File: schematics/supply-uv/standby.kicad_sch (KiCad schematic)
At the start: 108 parts, among them J5 CW2B-10A-T, K1 SRD-12VDC-SL-C, Q1 5N65F, Q2 IRLML5203, Q3 IRLML5203, Q4 IRLML5203, U10 TL331, U2 R7731, U3 EL817, U4 EL817, U5 L7805ABV, U6 L7805ABV, U7 TL431DBZ, U8 EL817, U9 TL432DBZ, Y1 B32022A3223M000

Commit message: Boards prepared to order
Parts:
- added TP3: Supply GND, Library:TestPoint_Plated_Hole_D1.0mm, symbol Connector:TestPoint
- TP10: renamed from TP8; footprint TestPoint:TestPoint_Pad_2.0x2.0mm -> TestPoint:TestPoint_Pad_1.0x1.0mm
- TP2: footprint TestPoint:TestPoint_Pad_2.0x2.0mm -> TestPoint:TestPoint_Pad_1.0x1.0mm
- TP5: renamed from TP4; footprint TestPoint:TestPoint_Pad_2.0x2.0mm -> TestPoint:TestPoint_Pad_1.0x1.0mm
- TP7: renamed from TP6; footprint TestPoint:TestPoint_Pad_2.0x2.0mm -> TestPoint:TestPoint_Pad_1.0x1.0mm
- renumbered C76 to C27, C27 to C28, C28 to C29, C29 to C30, R9 to R8, R8 to R9, TP9 to TP11, TP3 to TP4, TP5 to TP6, TP7 to TP8, TP35 to TP9
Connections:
- net HV_GND: now also TP3.1
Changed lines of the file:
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@@
 	(wire
 		(pts
+			(xy 87.63 236.22) (xy 111.76 236.22)
+		)
+		(stroke
+			(width 0)
+			(type default)
+		)
+	)
+	(wire
+		(pts
 			(xy 116.84 172.72) (xy 124.46 172.72)
 		)
@@
 	(wire
 		(pts
-			(xy 88.9 234.95) (xy 99.06 234.95)
+			(xy 88.9 224.79) (xy 99.06 224.79)
 		)
 		(stroke
@@
 		)
 	)
+	(hierarchical_label "HV_GND"
+		(shape input)
+		(at 87.63 236.22 180)
+		(fields_autoplaced yes)
+		(effects
+			(font
+				(size 1.27 1.27)
+			)
+			(justify right)
+		)
+	)
 	(hierarchical_label "VSYS1_VCC"
 		(shape input)
@@
 	(hierarchical_label "STB_VCC"
 		(shape input)
-		(at 88.9 234.95 180)
+		(at 88.9 224.79 180)
 		(fields_autoplaced yes)
 		(effects
@@
 		(dnp no)
 		(fields_autoplaced yes)
-		(property "Reference" "TP8"
+		(property "Reference" "TP10"
 			(at 163.83 34.7979 0)
 			(effects
@@
 			)
 		)
-		(property "Footprint" "TestPoint:TestPoint_Pad_2.0x2.0mm"
+		(property "Footprint" "TestPoint:TestPoint_Pad_1.0x1.0mm"
 			(at 166.37 39.37 0)
 			(effects
@@
 			(project ""
 				(path "/ef40850c-d0bf-4cba-961b-9aba418f8e73/14317b0a-1f8a-4d8b-b159-cbc20c410ffd"
-					(reference "TP8")
+					(reference "TP10")
 					(unit 1)
 				)
@@
 	(symbol
 		(lib_id "power:PWR_FLAG")
-		(at 99.06 234.95 0)
+		(at 99.06 224.79 0)
 		(unit 1)
 		(exclude_from_sim no)
@@
 		(fields_autoplaced yes)
 		(property "Reference" "#FLG03"
-			(at 99.06 233.045 0)
+			(at 99.06 222.885 0)
 			(effects
 				(font
@@
 		)
 		(property "Value" "PWR_FLAG"
-			(at 99.06 229.87 0)
+			(at 99.06 219.71 0)
 			(effects
 				(font
@@
 		)
 		(property "Footprint" ""
-			(at 99.06 234.95 0)
+			(at 99.06 224.79 0)
 			(effects
 				(font
@@
 		)
 		(property "Datasheet" "~"
-			(at 99.06 234.95 0)
+			(at 99.06 224.79 0)
 			(effects
 				(font
@@
 		)
 		(property "Description" "Special symbol for telling ERC where power comes from"
-			(at 99.06 234.95 0)
+			(at 99.06 224.79 0)
 			(effects
 				(font
@@
 		(dnp no)
 		(fields_autoplaced yes)
-		(property "Reference" "TP4"
+		(property "Reference" "TP5"
 			(at 114.3 245.6179 0)
 			(effects
@@
 			)
 		)
-		(property "Footprint" "TestPoint:TestPoint_Pad_2.0x2.0mm"
+		(property "Footprint" "TestPoint:TestPoint_Pad_1.0x1.0mm"
 			(at 116.84 250.19 0)
 			(effects
@@
 			(project "supply-uv"
 				(path "/ef40850c-d0bf-4cba-961b-9aba418f8e73/14317b0a-1f8a-4d8b-b159-cbc20c410ffd"
-					(reference "TP4")
+					(reference "TP5")
 					(unit 1)
 				)
@@
 		(on_board yes)
 		(dnp no)
-		(property "Reference" "R9"
+		(property "Reference" "R8"
 			(at 104.14 170.18 90)
 			(effects
@@
 			(project "supply-uv"
 				(path "/ef40850c-d0bf-4cba-961b-9aba418f8e73/14317b0a-1f8a-4d8b-b159-cbc20c410ffd"
-					(reference "R9")
+					(reference "R8")
 					(unit 1)
 				)
@@
 	)
 	(symbol
+		(lib_id "Connector:TestPoint")
+		(at 111.76 236.22 0)
+		(unit 1)
+		(exclude_from_sim no)
+		(in_bom yes)
+		(on_board yes)
+		(dnp no)
+		(fields_autoplaced yes)
+		(property "Reference" "TP3"
+			(at 114.3 231.6479 0)
+			(effects
+				(font
+					(size 1.27 1.27)
+				)
+				(justify left)
+			)
+		)
+		(property "Value" "Supply GND"
+			(at 114.3 234.1879 0)
+			(effects
+				(font
+					(size 1.27 1.27)
+				)
+				(justify left)
+			)
+		)
+		(property "Footprint" "Library:TestPoint_Plated_Hole_D1.0mm"
+			(at 116.84 236.22 0)
+			(effects
+				(font
+					(size 1.27 1.27)
+				)
+				(hide yes)
+			)
+		)
+		(property "Datasheet" "~"
+			(at 116.84 236.22 0)
+			(effects
+				(font
+					(size 1.27 1.27)
+				)
+				(hide yes)
+			)
+		)
+		(property "Description" "test point"
+			(at 111.76 236.22 0)
+			(effects
+				(font
+					(size 1.27 1.27)
+				)
+				(hide yes)
+			)
+		)
+		(pin "1"
+		)
+		(instances
+			(project "supply-uv"
+				(path "/ef40850c-d0bf-4cba-961b-9aba418f8e73/14317b0a-1f8a-4d8b-b159-cbc20c410ffd"
+					(reference "TP3")
+					(unit 1)
+				)
+			)
+		)
+	)
+	(symbol
 		(lib_id "Device:C_Polarized")
 		(at 370.84 135.89 0)
@@
 		(dnp no)
 		(fields_autoplaced yes)
-		(property "Reference" "C29"
+		(property "Reference" "C30"
 			(at 374.65 133.731 0)
 			(effects
@@
 			(project "supply-uv"
 				(path "/ef40850c-d0bf-4cba-961b-9aba418f8e73/14317b0a-1f8a-4d8b-b159-cbc20c410ffd"
-					(reference "C29")
+					(reference "C30")
 					(unit 1)
 				)
@@
 		(on_board yes)
 		(dnp no)
-		(property "Reference" "C27"
+		(property "Reference" "C28"
 			(at 340.36 148.59 0)
 			(effects
@@
 			(project "supply-uv"
 				(path "/ef40850c-d0bf-4cba-961b-9aba418f8e73/14317b0a-1f8a-4d8b-b159-cbc20c410ffd"
-					(reference "C27")
+					(reference "C28")
 					(unit 1)
 				)
@@
 		(dnp no)
 		(fields_autoplaced yes)
-		(property "Reference" "TP3"
+		(property "Reference" "TP4"
 			(at 114.3 239.2679 0)
 			(effects
@@
 			(project "supply-uv"
 				(path "/ef40850c-d0bf-4cba-961b-9aba418f8e73/14317b0a-1f8a-4d8b-b159-cbc20c410ffd"
-					(reference "TP3")
+					(reference "TP4")
 					(unit 1)
 				)
@@
 		(dnp no)
 		(fields_autoplaced yes)
-		(property "Reference" "TP9"
+		(property "Reference" "TP11"
 			(at 276.86 116.078 0)
 			(effects
@@
 			(project "supply-uv"
 				(path "/ef40850c-d0bf-4cba-961b-9aba418f8e73/14317b0a-1f8a-4d8b-b159-cbc20c410ffd"
-					(reference "TP9")
+					(reference "TP11")
 					(unit 1)
 				)
@@
 		(on_board yes)
 		(dnp no)
-		(property "Reference" "C76"
+		(property "Reference" "C27"
 			(at 281.178 369.57 0)
 			(effects
@@
 			(project "supply-uv"
 				(path "/ef40850c-d0bf-4cba-961b-9aba418f8e73/14317b0a-1f8a-4d8b-b159-cbc20c410ffd"
-					(reference "C76")
+					(reference "C27")
 					(unit 1)
 				)
@@
 		(dnp no)
 		(fields_autoplaced yes)
-		(property "Reference" "TP7"
+		(property "Reference" "TP8"
 			(at 114.3 268.4779 0)
 			(effects
@@
 			(project "supply-uv"
 				(path "/ef40850c-d0bf-4cba-961b-9aba418f8e73/14317b0a-1f8a-4d8b-b159-cbc20c410ffd"
-					(reference "TP7")
+					(reference "TP8")
 					(unit 1)
 				)
@@
 		(dnp no)
 		(fields_autoplaced yes)
-		(property "Reference" "TP5"
+		(property "Reference" "TP6"
 			(at 114.3 253.2379 0)
 			(effects
@@
 			(project "supply-uv"
 				(path "/ef40850c-d0bf-4cba-961b-9aba418f8e73/14317b0a-1f8a-4d8b-b159-cbc20c410ffd"
-					(reference "TP5")
+					(reference "TP6")
 					(unit 1)
 				)
@@
 		(on_board yes)
 		(dnp no)
-		(property "Reference" "TP35"
+		(property "Reference" "TP9"
 			(at 113.792 165.608 0)
 			(effects
@@
 			(project "supply-uv"
 				(path "/ef40850c-d0bf-4cba-961b-9aba418f8e73/14317b0a-1f8a-4d8b-b159-cbc20c410ffd"
-					(reference "TP35")
+					(reference "TP9")
 					(unit 1)
 				)
@@
 		(on_board yes)
 		(dnp no)
-		(property "Reference" "C28"
+		(property "Reference" "C29"
 			(at 345.44 238.125 0)
 			(effects
@@
 			(project "supply-uv"
 				(path "/ef40850c-d0bf-4cba-961b-9aba418f8e73/14317b0a-1f8a-4d8b-b159-cbc20c410ffd"
-					(reference "C28")
+					(reference "C29")
 					(unit 1)
 				)
@@
 		(dnp no)
 		(fields_autoplaced yes)
-		(property "Reference" "TP6"
+		(property "Reference" "TP7"
 			(at 114.3 260.8579 0)
 			(effects
@@
 			)
 		)
-		(property "Footprint" "TestPoint:TestPoint_Pad_2.0x2.0mm"
+		(property "Footprint" "TestPoint:TestPoint_Pad_1.0x1.0mm"
 			(at 116.84 265.43 0)
 			(effects
@@
 			(project "supply-uv"
 				(path "/ef40850c-d0bf-4cba-961b-9aba418f8e73/14317b0a-1f8a-4d8b-b159-cbc20c410ffd"
-					(reference "TP6")
+					(reference "TP7")
 					(unit 1)
 				)
@@
 		(on_board yes)
 		(dnp no)
-		(property "Reference" "R8"
+		(property "Reference" "R9"
 			(at 102.87 133.35 0)
 			(effects
@@
 			(project "supply-uv"
 				(path "/ef40850c-d0bf-4cba-961b-9aba418f8e73/14317b0a-1f8a-4d8b-b159-cbc20c410ffd"
-					(reference "R8")
+					(reference "R9")
 					(unit 1)
 				)
@@
 			)
 		)
-		(property "Footprint" "TestPoint:TestPoint_Pad_2.0x2.0mm"
+		(property "Footprint" "TestPoint:TestPoint_Pad_1.0x1.0mm"
 			(at 96.52 143.51 0)
 			(effects

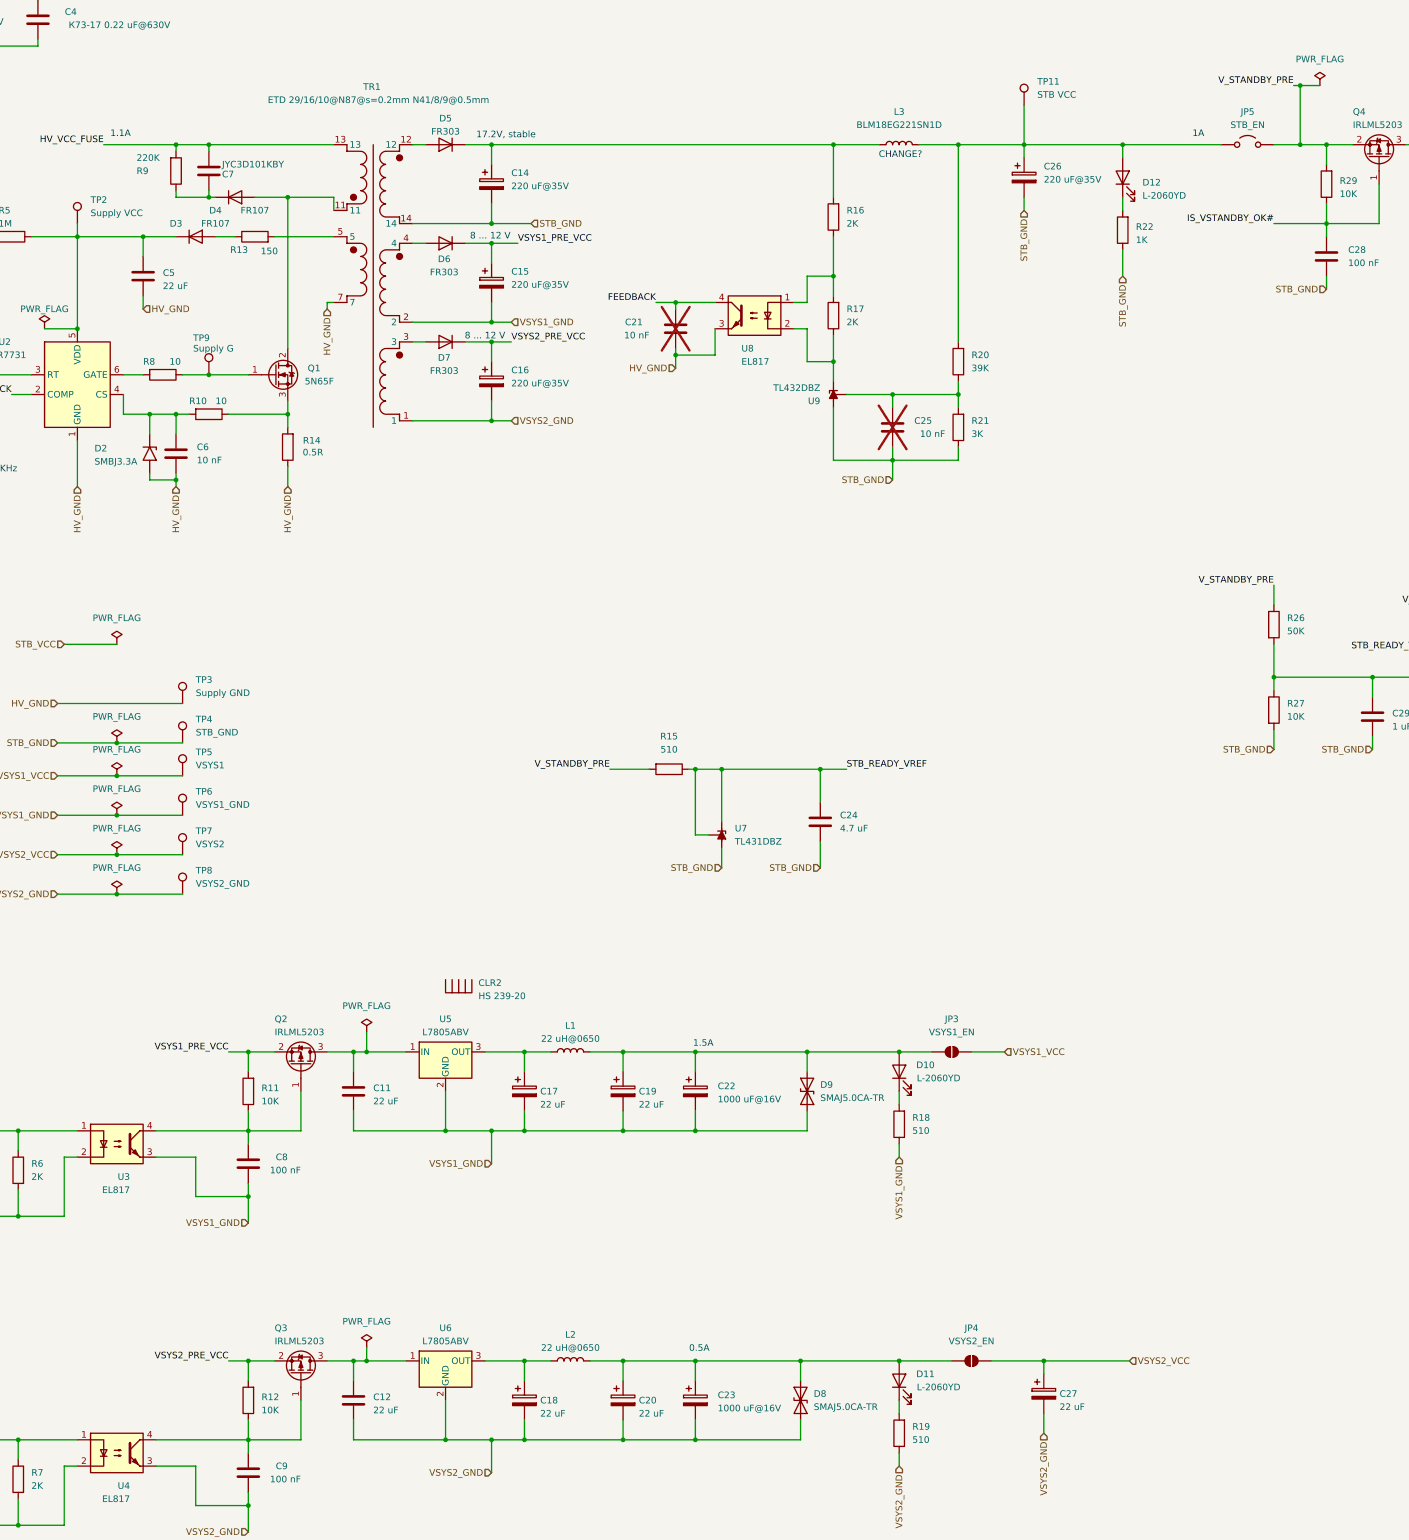
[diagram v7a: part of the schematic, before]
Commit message: power board works (except power output driver, not tested yet), I ready to solder control board
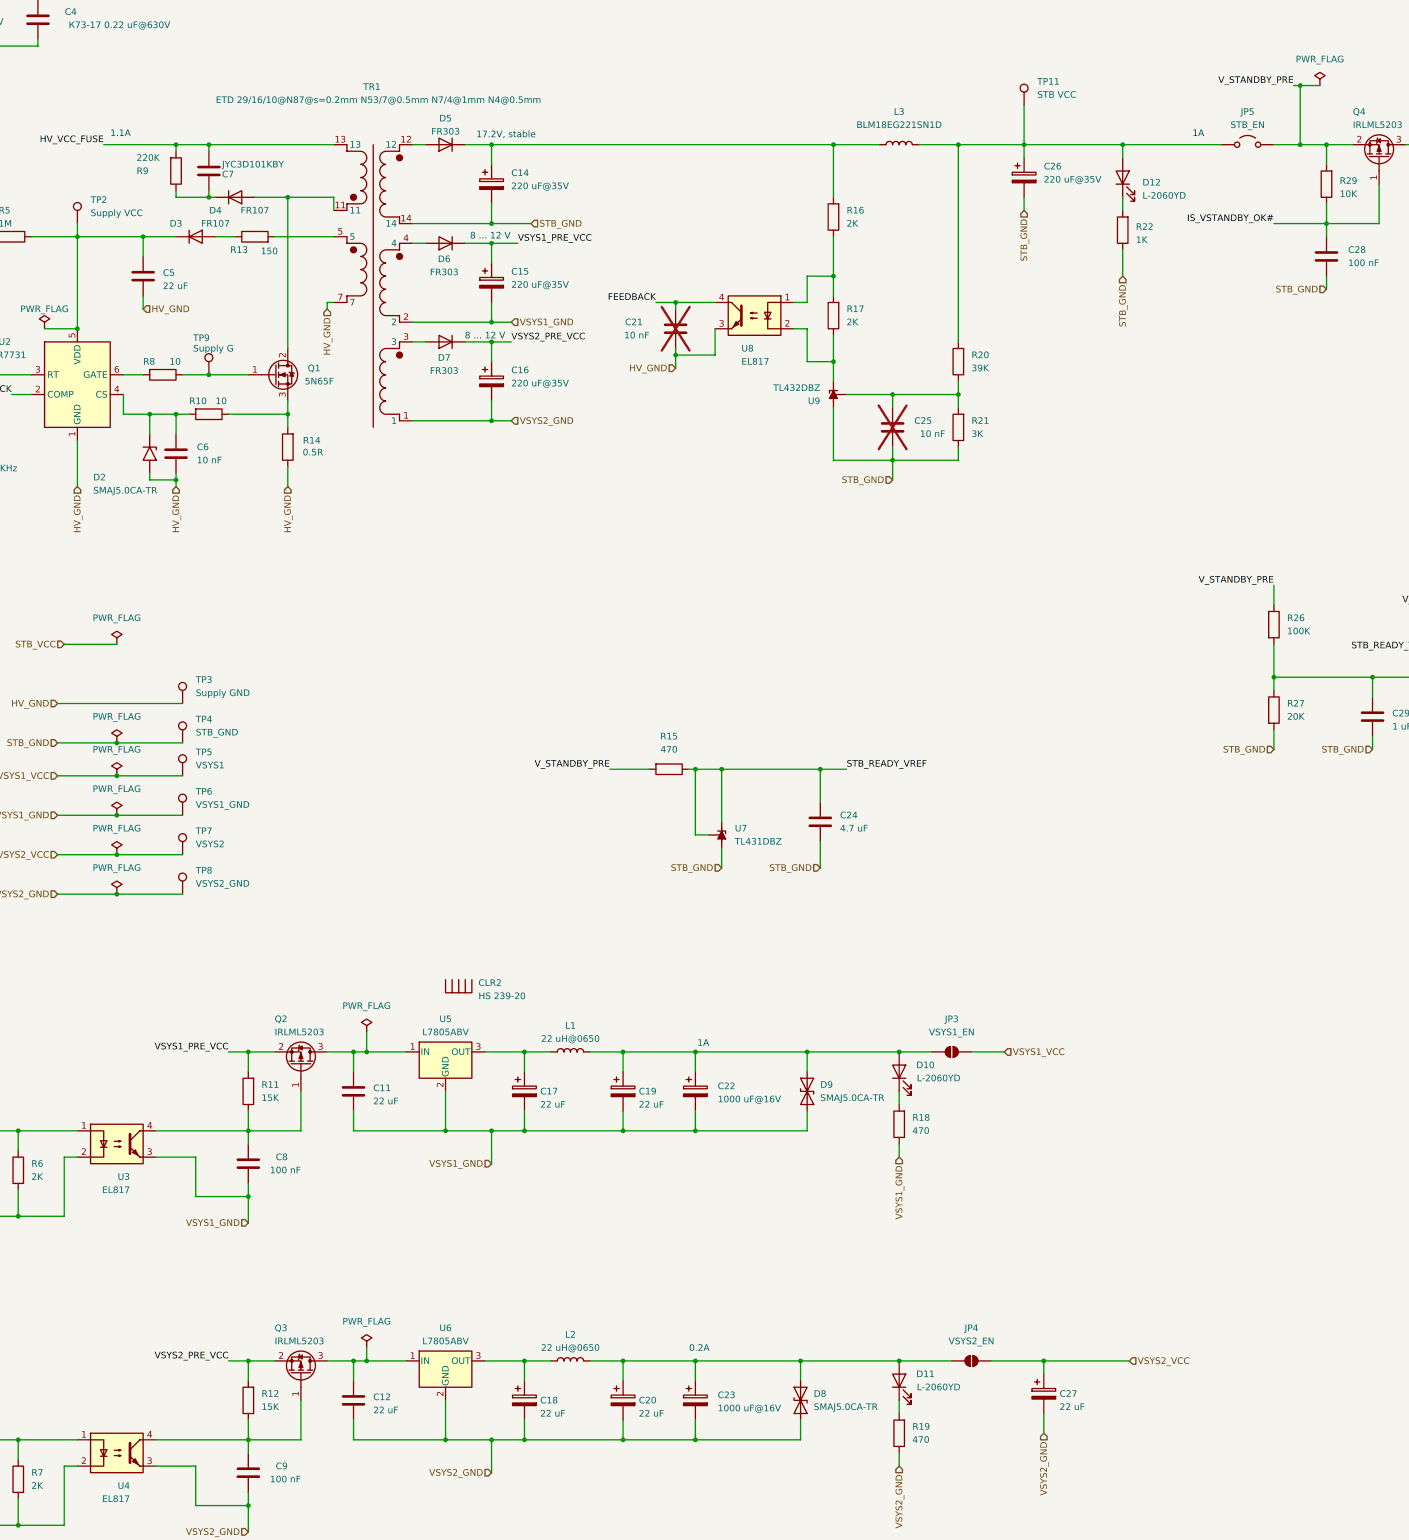
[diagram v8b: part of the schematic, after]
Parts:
- D2: value SMBJ3.3A -> SMAJ5.0CA-TR
- R11, R12: value 10K -> 15K
- R15, R18, R19: value 510 -> 470
- R26: value 50K -> 100K
- R27: value 10K -> 20K
- TR1: value ETD 29/16/10@N87@s=0.2mm N41/8/9@0.5mm -> ETD 29/16/10@N87@s=0.2mm N53/7@0.5mm N7/4@1mm N4@0.5mm
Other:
- note added: "0.2A"
- note removed: "0.5A"
- note removed: "1.5A"
- note removed: "CHANGE?"
